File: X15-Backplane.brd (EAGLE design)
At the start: 160 x 100 mm, 37 parts, among them J3 IPL1-103-01-L-S-K, J4 IPL1-104-01-X-S-K

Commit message: Minor chnages to clean up some traces
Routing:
- net NRST: track 360.9 -> 330.9 mm
- net 3V3: track 430.6 -> 427.2 mm
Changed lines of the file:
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@@
 <contactref element="PI_SHIELD_CONN1" pad="12"/>
 <contactref element="D7" pad="A"/>
-<via x="80.772" y="26.162" extent="1-16" drill="0.8"/>
+<via x="80.772" y="22.098" extent="1-16" drill="0.8"/>
 <wire x1="39.116" y1="22.098" x2="37.084" y2="20.066" width="0.762" layer="1"/>
-<wire x1="80.772" y1="26.162" x2="78.232" y2="26.162" width="0.762" layer="1"/>
-<wire x1="78.232" y1="26.162" x2="74.168" y2="22.098" width="0.762" layer="1"/>
-<wire x1="74.168" y1="22.098" x2="39.116" y2="22.098" width="0.762" layer="1"/>
+<wire x1="80.772" y1="22.098" x2="39.116" y2="22.098" width="0.762" layer="1"/>
 <wire x1="156.718" y1="83.312" x2="156.718" y2="14.478" width="0.762" layer="16"/>
 <wire x1="156.718" y1="14.478" x2="154.686" y2="12.446" width="0.762" layer="16"/>
@@
 <wire x1="32.004" y1="70.612" x2="30.988" y2="69.596" width="0.762" layer="16"/>
 <wire x1="33.02" y1="86.614" x2="33.02" y2="71.628" width="0.762" layer="16"/>
-<wire x1="80.772" y1="26.162" x2="83.058" y2="26.162" width="0.762" layer="16"/>
-<wire x1="99.838" y1="9.382" x2="83.058" y2="26.162" width="0.762" layer="16"/>
+<wire x1="80.772" y1="22.098" x2="87.122" y2="22.098" width="0.762" layer="16"/>
+<wire x1="99.838" y1="9.382" x2="87.122" y2="22.098" width="0.762" layer="16"/>
 <wire x1="101.902" y1="9.382" x2="101.902" y2="10.97" width="0.762" layer="16"/>
 <wire x1="103.378" y1="12.446" x2="101.902" y2="10.97" width="0.762" layer="16"/>
@@
 <wire x1="103.886" y1="3.302" x2="147.96403125" y2="3.302" width="0.2032" layer="16"/>
 <wire x1="147.96403125" y1="3.302" x2="158.115" y2="13.45296875" width="0.2032" layer="16"/>
-<wire x1="158.115" y1="85.979" x2="154.686" y2="89.408" width="0.2032" layer="16"/>
-<via x="154.686" y="89.408" extent="1-16" drill="0.35"/>
-<wire x1="154.686" y1="89.408" x2="153.67" y2="90.424" width="0.2032" layer="1"/>
-<wire x1="153.67" y1="90.424" x2="152.654" y2="90.424" width="0.2032" layer="1"/>
-<wire x1="145.796" y1="83.566" x2="145.796" y2="76.454" width="0.2032" layer="1"/>
-<wire x1="145.796" y1="76.454" x2="145.168" y2="75.826" width="0.2032" layer="1"/>
-<wire x1="145.168" y1="75.826" x2="92.456" y2="75.826" width="0.2032" layer="1"/>
-<wire x1="158.115" y1="13.45296875" x2="158.115" y2="85.979" width="0.2032" layer="16"/>
-<wire x1="152.654" y1="90.424" x2="145.796" y2="83.566" width="0.2032" layer="1"/>
+<wire x1="158.115" y1="62.611" x2="157.988" y2="62.738" width="0.2032" layer="16"/>
+<via x="157.988" y="62.738" extent="1-16" drill="0.35"/>
+<wire x1="157.988" y1="62.738" x2="144.9" y2="75.826" width="0.2032" layer="1"/>
+<wire x1="144.9" y1="75.826" x2="92.456" y2="75.826" width="0.2032" layer="1"/>
+<wire x1="158.115" y1="13.45296875" x2="158.115" y2="62.611" width="0.2032" layer="16"/>
 <wire x1="66.294" y1="69.596" x2="48.602" y2="69.596" width="0.2032" layer="1"/>
 <wire x1="70.564" y1="75.692" x2="67.056" y2="72.184" width="0.2032" layer="1"/>

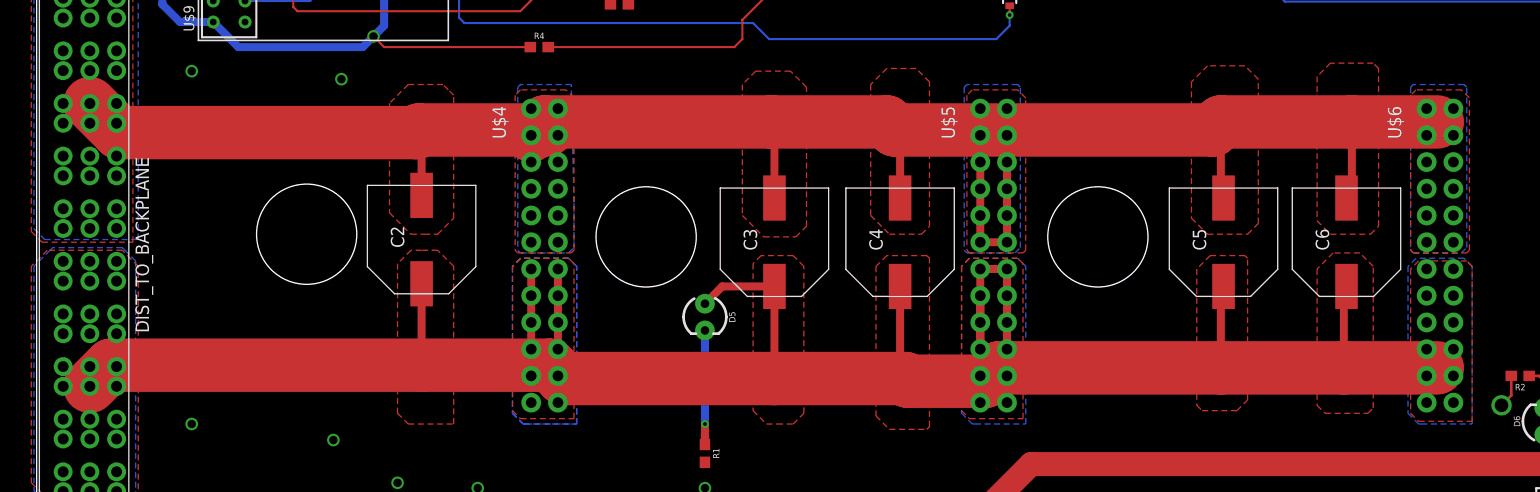
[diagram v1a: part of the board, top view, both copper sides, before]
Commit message: 12V Wire Fixed
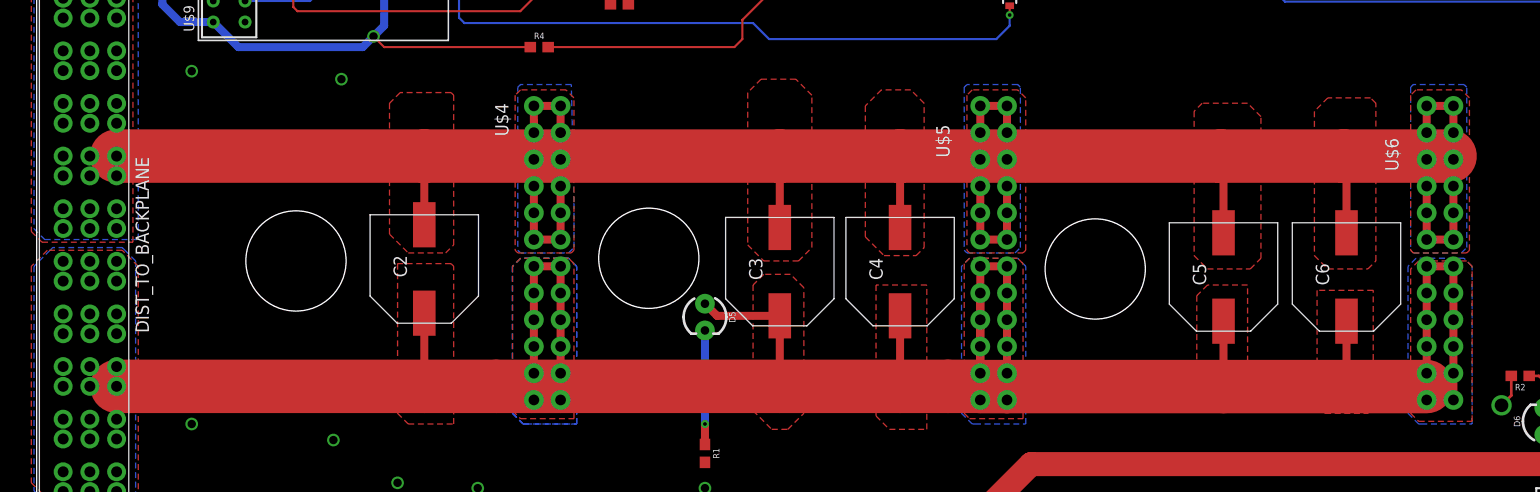
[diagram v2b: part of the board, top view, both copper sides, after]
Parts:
- moved C5 3.30 mm to (112.8, 47.8)
- moved C6 3.30 mm to (124.5, 47.8)
- moved C3 2.84 mm to (70.6, 48.3)
- moved C2 2.81 mm to (36.8, 48.5)
- moved C4 2.79 mm to (82.0, 48.3)
- moved U$4 0.36 mm to (10.9, 101.1)
- moved U$5 0.25 mm to (53.3, 101.1)
- moved U$6 0.25 mm to (95.8, 101.1)
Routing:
- net 12VGND: track 194.3 -> 254.8 mm
- net 12V: track 261.3 -> 264.3 mm

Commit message: Updated
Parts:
- renumbered ESC_CONTROL1 to ESC_CONTROLLER, J3 to ROBOT_CONN, J4 to 7.4V_CONN, PXC-8-RA-1 to SOLENOID, U$9 to DATA_CON_CONN
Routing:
- net ROBOT_ARM: track 102.0 -> 99.9 mm
- net NRST: track 330.9 -> 332.5 mm

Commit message: Hmm
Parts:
- removed PXC-8-RA-1778683: PXC-8-RA-1778683, X15-Backplane Parts:PXC-8-RA-1778683
- R1: value 150,000,000 -> 1500
- moved R1 1.14 mm to (64.5, 31.5), turned to 0 degrees
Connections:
- removed net PROG_1: PXC-8-RA-1778683.7
- removed net PROG_2: PXC-8-RA-1778683.6
- removed net PROG_3: PXC-8-RA-1778683.5
- removed net SWCLK_IN: PXC-8-RA-1778683.2
- removed net SWDIO_IN: PXC-8-RA-1778683.1
- net 3V3: no longer PXC-8-RA-1778683.4
- net GND: no longer PXC-8-RA-1778683.8
- net NRST: no longer PXC-8-RA-1778683.3
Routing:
- net NRST: track 332.5 -> 230.8 mm, vias 2 -> 1
- net 3V3: track 427.2 -> 340.7 mm, vias 4 -> 3
- net 7.4VGND: vias 1 -> 0
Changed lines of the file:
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@@
 <attribute name="SPICEPREFIX" value="X" x="37.846" y="263.652" size="1.778" layer="27" rot="R180" display="off"/>
-</element>
-<element name="PXC-8-RA-1778683" library="X15-Backplane Parts" package="PXC-8-RA-1778683" package3d_urn="urn:adsk.eagle:package:25224885/2" value="PXC-8-RA-1778683" x="11.938" y="15.748" smashed="yes">
-<attribute name="SPICEPREFIX" value="X" x="88.138" y="-153.162" size="1.778" layer="27" display="off"/>
 </element>
 <element name="R4" library="SparkFun-Resistors" library_urn="urn:adsk.eagle:library:532" package="0603" package3d_urn="urn:adsk.eagle:package:39650/1" value="10k" x="47.752" y="69.596" smashed="yes">
@@
 <attribute name="VALUE" x="61.214" y="43.942" size="0.6096" layer="27" font="vector" ratio="20" rot="R270" align="top-center"/>
 </element>
-<element name="R1" library="SparkFun-Resistors" library_urn="urn:adsk.eagle:library:532" package="0603" package3d_urn="urn:adsk.eagle:package:39650/1" value="150,000,000" x="63.5" y="30.988" smashed="yes" rot="R270">
-<attribute name="NAME" x="64.262" y="30.988" size="0.6096" layer="25" font="vector" ratio="20" rot="R270" align="bottom-center"/>
-<attribute name="PROD_ID" value=" " x="69.85" y="36.068" size="1.778" layer="27" rot="R270" display="off"/>
-<attribute name="VALUE" x="62.738" y="30.988" size="0.6096" layer="27" font="vector" ratio="20" rot="R270" align="top-center"/>
-</element>
 <element name="D7" library="SparkFun-LED" library_urn="urn:adsk.eagle:library:529" package="LED_3MM" package3d_urn="urn:adsk.eagle:package:39361/1" value="" x="145.288" y="9.652" smashed="yes" rot="R180">
 <attribute name="NAME" x="145.288" y="7.366" size="0.6096" layer="25" font="vector" ratio="20" rot="R180" align="bottom-center"/>
@@
 <attribute name="VALUE" x="139.954" y="81.534" size="0.6096" layer="27" font="vector" ratio="20" rot="R180" align="top-center"/>
 </element>
+<element name="R1" library="SparkFun-Resistors" library_urn="urn:adsk.eagle:library:532" package="0603" package3d_urn="urn:adsk.eagle:package:39650/1" value="1500" x="64.516" y="31.496" smashed="yes">
+<attribute name="NAME" x="64.516" y="32.258" size="0.6096" layer="25" font="vector" ratio="20" align="bottom-center"/>
+<attribute name="PROD_ID" value=" " x="64.516" y="31.496" size="1.778" layer="27" display="off"/>
+<attribute name="VALUE" x="64.516" y="30.48" size="0.6096" layer="27" font="vector" ratio="20" align="top-center"/>
+</element>
 </elements>
 <signals>
-<signal name="SWDIO_IN">
-<contactref element="PXC-8-RA-1778683" pad="1"/>
-</signal>
 <signal name="SWDIO_4">
 <contactref element="DATA_CON_CONN" pad="6"/>
 </signal>
-<signal name="PROG_3">
-<contactref element="PXC-8-RA-1778683" pad="5"/>
-</signal>
-<signal name="PROG_1">
-<contactref element="PXC-8-RA-1778683" pad="7"/>
-</signal>
 <signal name="SWCLK_4">
 <contactref element="DATA_CON_CONN" pad="8"/>
 </signal>
-<signal name="SWCLK_IN">
-<contactref element="PXC-8-RA-1778683" pad="2"/>
-</signal>
 <signal name="3V3">
-<contactref element="PXC-8-RA-1778683" pad="4"/>
 <contactref element="R4" pad="1"/>
 <contactref element="U$8" pad="04"/>
@@
 <contactref element="PI_SHIELD_CONN1" pad="12"/>
 <contactref element="D7" pad="A"/>
-<via x="80.772" y="22.098" extent="1-16" drill="0.8"/>
-<wire x1="39.116" y1="22.098" x2="37.084" y2="20.066" width="0.762" layer="1"/>
-<wire x1="80.772" y1="22.098" x2="39.116" y2="22.098" width="0.762" layer="1"/>
 <wire x1="156.718" y1="83.312" x2="156.718" y2="14.478" width="0.762" layer="16"/>
 <wire x1="156.718" y1="14.478" x2="154.686" y2="12.446" width="0.762" layer="16"/>
@@
 <wire x1="32.004" y1="70.612" x2="30.988" y2="69.596" width="0.762" layer="16"/>
 <wire x1="33.02" y1="86.614" x2="33.02" y2="71.628" width="0.762" layer="16"/>
-<wire x1="80.772" y1="22.098" x2="87.122" y2="22.098" width="0.762" layer="16"/>
-<wire x1="99.838" y1="9.382" x2="87.122" y2="22.098" width="0.762" layer="16"/>
 <wire x1="101.902" y1="9.382" x2="101.902" y2="10.97" width="0.762" layer="16"/>
 <wire x1="103.378" y1="12.446" x2="101.902" y2="10.97" width="0.762" layer="16"/>
@@
 <wire x1="149.098" y1="10.414" x2="148.336" y2="9.652" width="0.3048" layer="1"/>
 <wire x1="148.336" y1="9.652" x2="146.558" y2="9.652" width="0.3048" layer="1"/>
-<wire x1="37.084" y1="20.066" x2="22.86" y2="20.066" width="0.762" layer="1"/>
-<wire x1="22.86" y1="20.066" x2="21.538" y2="21.388" width="0.762" layer="1"/>
-<wire x1="21.538" y1="21.388" x2="21.538" y2="22.948" width="0.762" layer="1"/>
 <via x="32.004" y="70.612" extent="1-16" drill="0.8"/>
 <wire x1="32.004" y1="70.612" x2="33.02" y2="69.596" width="0.2032" layer="1"/>
@@
 </signal>
 <signal name="NRST">
-<contactref element="PXC-8-RA-1778683" pad="3"/>
 <contactref element="D4" pad="C"/>
 <contactref element="R4" pad="2"/>
 <contactref element="U$7" pad="2"/>
 <contactref element="ESC_CONTROLLER" pad="6"/>
-<wire x1="19.038" y1="22.948" x2="19.038" y2="9.918" width="0.2032" layer="16"/>
-<wire x1="19.038" y1="9.918" x2="21.082" y2="7.874" width="0.2032" layer="16"/>
-<wire x1="21.082" y1="7.874" x2="39.116" y2="7.874" width="0.2032" layer="16"/>
-<wire x1="39.116" y1="7.874" x2="42.926" y2="4.064" width="0.2032" layer="16"/>
-<wire x1="42.926" y1="4.064" x2="101.6" y2="4.064" width="0.2032" layer="16"/>
-<wire x1="101.6" y1="4.064" x2="102.362" y2="3.302" width="0.2032" layer="16"/>
-<wire x1="102.362" y1="3.302" x2="103.886" y2="3.302" width="0.2032" layer="16"/>
-<wire x1="103.886" y1="3.302" x2="147.96403125" y2="3.302" width="0.2032" layer="16"/>
+<wire x1="105.918" y1="3.302" x2="147.96403125" y2="3.302" width="0.2032" layer="16"/>
 <wire x1="147.96403125" y1="3.302" x2="158.369" y2="13.70696875" width="0.2032" layer="16"/>
 <wire x1="158.369" y1="62.357" x2="157.988" y2="62.738" width="0.2032" layer="16"/>
@@
 <wire x1="67.056" y1="70.358" x2="66.294" y2="69.596" width="0.2032" layer="1"/>
 <wire x1="67.056" y1="72.184" x2="67.056" y2="70.358" width="0.2032" layer="1"/>
-<via x="103.886" y="3.302" extent="1-16" drill="0.35"/>
-<wire x1="103.886" y1="3.302" x2="103.886" y2="7.366" width="0.2032" layer="1"/>
 <wire x1="103.886" y1="7.366" x2="103.902" y2="7.382" width="0.2032" layer="1"/>
 <wire x1="70.564" y1="75.692" x2="70.698" y2="75.826" width="0.2032" layer="1"/>
@@
 <wire x1="155.321" y1="63.119" x2="155.702" y2="62.738" width="0.2032" layer="1"/>
 <wire x1="155.702" y1="62.738" x2="157.988" y2="62.738" width="0.2032" layer="1"/>
-</signal>
-<signal name="PROG_2">
-<contactref element="PXC-8-RA-1778683" pad="6"/>
+<wire x1="105.918" y1="3.302" x2="105.664" y2="3.302" width="0.2032" layer="16"/>
+<wire x1="105.664" y1="3.302" x2="103.886" y2="5.08" width="0.2032" layer="16"/>
+<wire x1="103.886" y1="5.08" x2="103.886" y2="7.366" width="0.2032" layer="16"/>
+<wire x1="103.886" y1="7.366" x2="103.902" y2="7.382" width="0.1524" layer="16"/>
 </signal>
 <signal name="CAN_H">
@@
 <contactref element="7.4V_CONN" pad="03"/>
 <contactref element="7.4V_CONN" pad="04"/>
-<wire x1="6.858" y1="6.858" x2="6.858" y2="4.318" width="2.286" layer="16"/>
-<wire x1="6.858" y1="4.318" x2="26.162" y2="4.318" width="2.286" layer="16"/>
-<via x="26.162" y="4.318" extent="1-16" drill="2.54"/>
+<wire x1="6.858" y1="6.858" x2="6.858" y2="4.318" width="2.286" layer="1"/>
+<wire x1="6.858" y1="4.318" x2="26.162" y2="4.318" width="2.286" layer="1"/>
 <wire x1="44.06" y1="9.008" x2="52.578" y2="9.008" width="2.286" layer="1"/>
 <wire x1="26.162" y1="4.318" x2="39.37" y2="4.318" width="2.286" layer="1"/>
@@
 <contactref element="R3" pad="2"/>
 <contactref element="R7" pad="2"/>
-<contactref element="R1" pad="2"/>
 <contactref element="R2" pad="2"/>
 <polygon width="0.1524" layer="1" rank="5">
@@
 <contactref element="U$8" pad="05"/>
 <contactref element="U$8" pad="06"/>
-<contactref element="PXC-8-RA-1778683" pad="8"/>
 <contactref element="DATA_CON_CONN" pad="2"/>
 <contactref element="DATA_CON_CONN" pad="3"/>
@@
 <via x="36.068" y="76.454" extent="1-16" drill="0.8"/>
 <via x="44.196" y="92.964" extent="1-16" drill="0.8"/>
+<contactref element="R1" pad="2"/>
 </signal>
 <signal name="SWCLK">
@@
 <signal name="N$2">
 <contactref element="D5" pad="K"/>
-<contactref element="R1" pad="1"/>
 <wire x1="63.5" y1="42.672" x2="63.5" y2="33.782" width="0.762" layer="16"/>
 <via x="63.5" y="33.782" extent="1-16" drill="0.35"/>
-<wire x1="63.5" y1="33.782" x2="63.5" y2="31.838" width="0.762" layer="1"/>
+<contactref element="R1" pad="1"/>
+<wire x1="63.5" y1="33.782" x2="63.5" y2="31.662" width="0.762" layer="1"/>
+<wire x1="63.5" y1="31.662" x2="63.666" y2="31.496" width="0.762" layer="1"/>
 </signal>
 <signal name="N$3">

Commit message: update
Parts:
- removed D4: 0.5A/40V/420mV, SparkFun-DiscreteSemi:SOD-323
- removed R4: 10k, SparkFun-Resistors:0603
- removed U$7: (no value), X15-Backplane Parts:DISCRETECOMPONENTS_SW_2512
- added U1: ULN2003AD, X15-Pi-Shield-Parts:16-SOIC
- moved SOLENOID 10.4 mm to (90.7, 105.2)
- moved CAN_DEBUG 9.16 mm to (56.4, 98.0), turned to 180 degrees
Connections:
- new net GPIO1: PI_SHIELD_CONN1.1, U1.1
- new net GPIO2: PI_SHIELD_CONN1.3, U1.2
- new net GPIO3: PI_SHIELD_CONN1.5, U1.3
- new net GPIO4: PI_SHIELD_CONN1.7, U1.4
- new net GPIO5: PI_SHIELD_CONN1.9, U1.5
- new net GPIO6: PI_SHIELD_CONN1.11, U1.6
- new net ROBOT_ARM_2: PI_SHIELD_CONN1.16
- net 12V: now also U1.9
- net 3V3: no longer R4.1
- net GND: now also U1.8; no longer U$7.1
- net NRST: no longer D4.C, R4.2, U$7.2
- net NRST_4: no longer D4.A
- net SOL1_1: now also U1.16; no longer PI_SHIELD_CONN1.1
- net SOL2_1: now also U1.15; no longer PI_SHIELD_CONN1.3
- net SOL3_1: now also U1.14; no longer PI_SHIELD_CONN1.5
- net SOL4_1: now also U1.13; no longer PI_SHIELD_CONN1.7
- net SOL5_1: now also U1.12; no longer PI_SHIELD_CONN1.9
- net SOL6_1: now also U1.11; no longer PI_SHIELD_CONN1.11
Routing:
- net NRST: track 230.8 -> 0.00 mm, vias 1 -> 0
- net NRST_4: track 91.7 -> 0.00 mm, vias 2 -> 0
- net CAN_H: track 285.9 -> 299.7 mm, vias 1 -> 7
- net 12L_GND: track 123.2 -> 113.8 mm, vias 1 -> 3
- net SOL6_1: track 37.8 -> 47.1 mm
- net SOL5_1: track 43.9 -> 53.1 mm
- net SOL3_1: track 57.0 -> 65.6 mm
- net SOL2_1: track 63.4 -> 71.7 mm
- net SOL1_1: track 69.7 -> 77.7 mm
- net SOL4_1: track 51.1 -> 58.9 mm
- net 12V_L: track 141.0 -> 135.9 mm, vias 4 -> 2
- net 3V3: track 340.7 -> 344.0 mm, vias 3 -> 6
- net 5V: track 162.7 -> 164.8 mm, vias 0 -> 2
- net CAN_L: track 285.7 -> 287.1 mm, vias 5 -> 6

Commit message: Hmm
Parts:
- D5, D6, D7, D8: device SparkFun-LED:LED_3MM -> SparkFun-LED:LED-0603
- R1: value 1500 -> 600
- R2: value 1500 -> 370
- R3: value 1500 -> 150
- R7: value 1500 -> 250
- ROBOT_CONN: value IPL1-103-01-L-S-K -> IPL1-104-01-X-S-K; device X15-Backplane Parts:SAMTEC_IPL1-103-01-L-S-K -> X15-Backplane Parts:SAMTEC_IPL1-104-01-X-S-K
- moved U1 139.0 mm to (101.3, 79.5), turned to 180 degrees
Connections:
- net 12V: no longer U1.9
- net 12V_L: now also U1.9; no longer PI_SHIELD_CONN1.2, PI_SHIELD_CONN1.4
- net N$1: now also D6.C; no longer D6.K
- net N$2: now also D5.C; no longer D5.K
- net N$3: now also D7.C; no longer D7.K
- net N$5: now also D8.C; no longer D8.K
- net ROBOT_ARM_2: now also ROBOT_CONN.04
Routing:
- net ROBOT_ARM_2: track 0.00 -> 110.8 mm, vias 0 -> 1
- net SOL1_1: track 77.7 -> 39.3 mm
- net GPIO1: track 0.00 -> 38.3 mm
- net 12V_L: track 135.9 -> 98.5 mm, vias 2 -> 3
- net SOL2_1: track 71.7 -> 36.2 mm
- net GPIO2: track 0.00 -> 35.2 mm
- net SOL3_1: track 65.6 -> 33.4 mm
- net GPIO3: track 0.00 -> 32.0 mm
- net SOL4_1: track 58.9 -> 30.2 mm
- net GPIO4: track 0.00 -> 28.7 mm
- net SOL5_1: track 53.1 -> 27.0 mm
- net GPIO5: track 0.00 -> 25.4 mm
- net SOL6_1: track 47.1 -> 24.1 mm
- net GPIO6: track 0.00 -> 22.2 mm
- net 7.4V: track 167.4 -> 164.6 mm, vias 0 -> 1
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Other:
- board text added: "X15 Backplane Bryce Sasser Minh Nguyen Katherine Sandys Rachel Livesay Hyunseok Hong"

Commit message: clearance fixed
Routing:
- net GND: track 6.39 -> 46.1 mm, vias 14 -> 17
